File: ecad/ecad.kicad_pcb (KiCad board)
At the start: 4 copper layers, 87 x 83 mm, 82 parts, among them J1 JTAG, J2 USB_C, SW1 Cherry MX, SW10 RotaryEncoder_Switch, SW11 RotaryEncoder_Switch, SW12 Cherry MX, SW13 Cherry MX, SW14 Cherry MX, SW15 RESET, SW2 Cherry MX, SW3 Cherry MX, SW4 Cherry MX, SW5 Cherry MX, SW6 Cherry MX, SW7 Cherry MX, SW8 Cherry MX, SW9 Cherry MX, U1 AP2112K-3.3, U2 RP2040, U4 SN74LV1T34DBV, U5 W25Q128JVP, Y1 12MHz

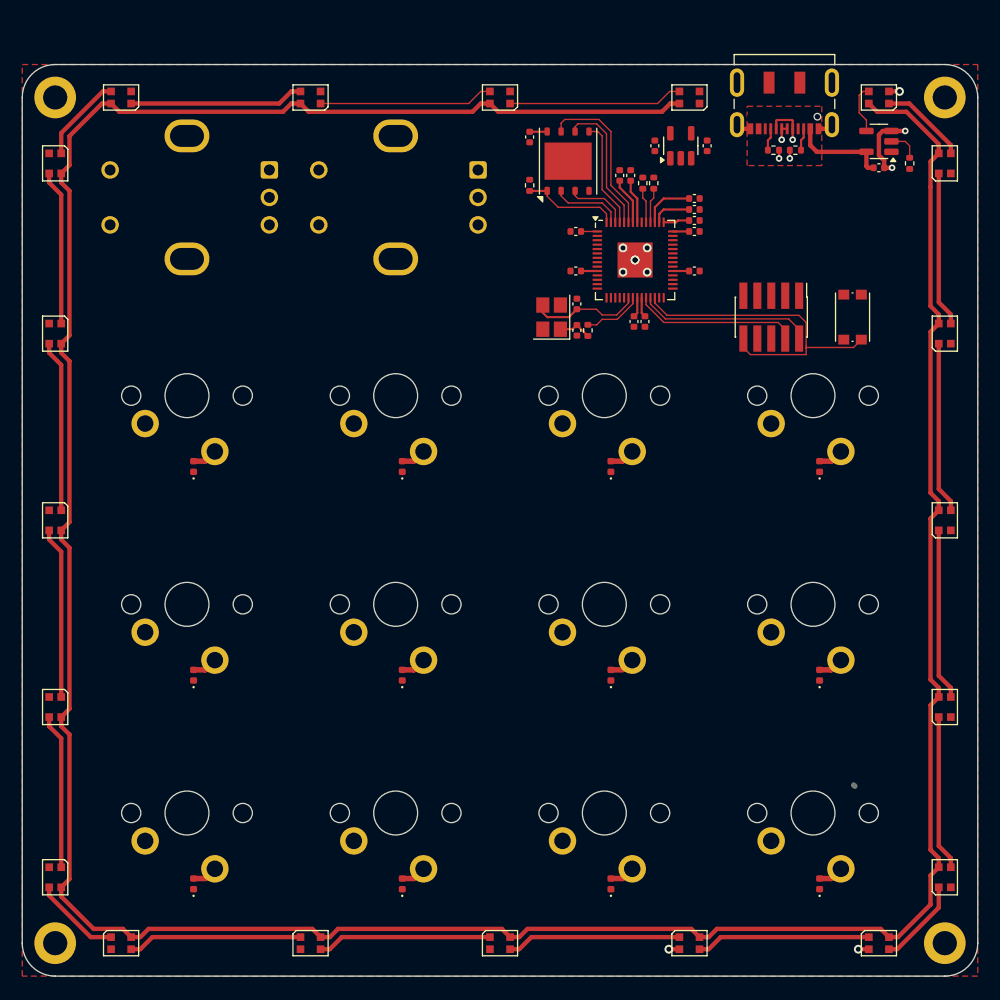
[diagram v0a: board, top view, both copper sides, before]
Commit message: feat(ecad): change pcb size to have constant margin
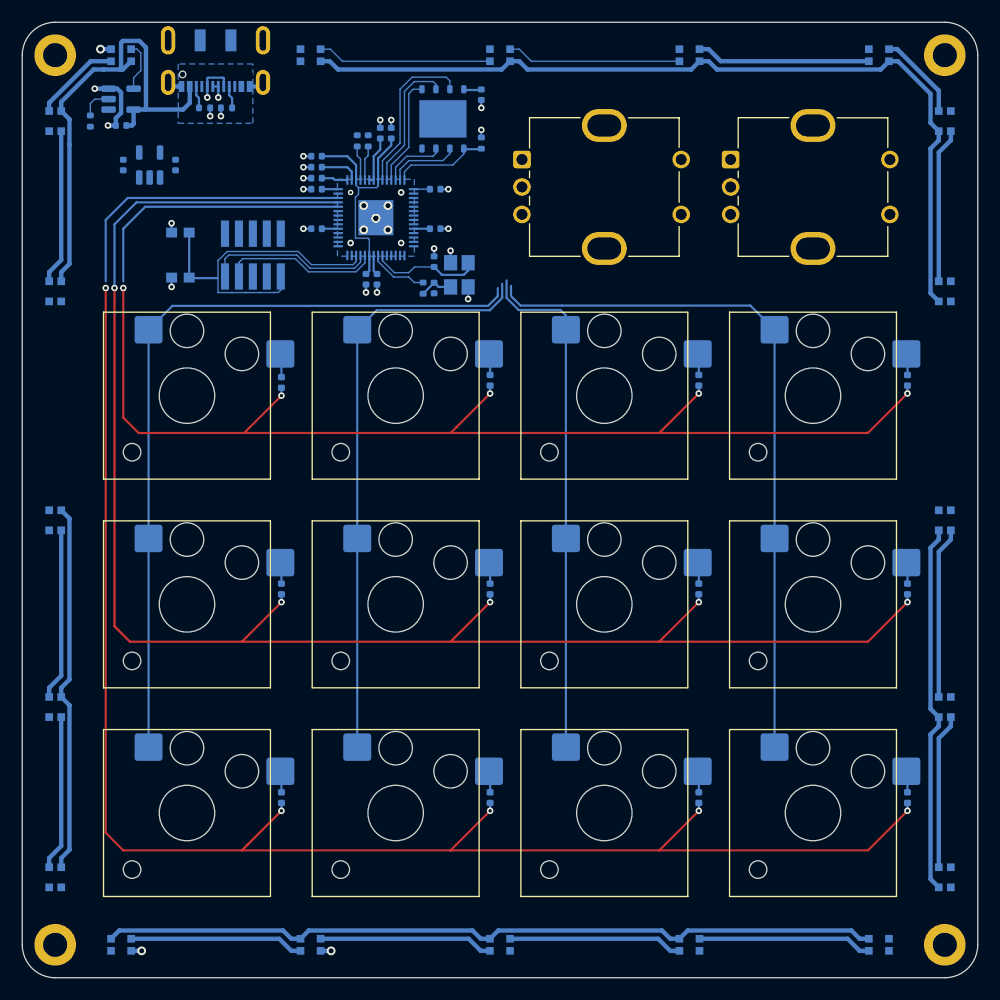
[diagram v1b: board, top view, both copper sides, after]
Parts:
- C1, C10, C11, C12, C13, C14, C15, C16, C17, C18, C2, C3, C4, C5, C6, C7, C8, D1, D10, D11, D12, D13, D14, D15, D16, D17, D18, D19, D2, D20, D21, D22, D23, D24, D25, D26, D27, D28, D29, D3, D30, D31, D32, D4, D5, D6, D7, D8, D9, H1, H2, H3, H4, J1, J2, R1, R2, R3, R4, R5, R6, R7, SW15, U1, U2, U4, U5, Y1: moved to B.Cu
- SW1, SW12, SW13, SW14, SW2, SW3, SW4, SW5, SW6, SW7, SW8, SW9: footprint PCM_Switch_Keyboard_Cherry_MX:SW_Cherry_MX_PCB_1.00u -> PCM_Switch_Keyboard_Hotswap_Kailh:SW_Hotswap_Kailh_Choc_V2; moved to F.Cu
- SW10, SW11: moved to F.Cu
- moved D15 81.1 mm to (147.0, 81.2)
- moved D19 81.1 mm to (147.0, 96.7)
- moved D25 81.1 mm to (66.0, 96.7)
- moved D29 81.1 mm to (66.0, 81.2)
- moved H1 81.1 mm to (147.0, 75.2), turned to 180 degrees
- moved H2 81.1 mm to (66.0, 75.2), turned to 180 degrees
- moved H3 81.0 mm to (147.0, 156.2), turned to 180 degrees
- moved H4 81.0 mm to (66.0, 156.2), turned to 180 degrees
- moved D13 81.0 mm to (66.0, 150.0)
- moved D17 81.0 mm to (66.0, 134.5)
- moved D21 81.0 mm to (66.0, 117.5)
- moved D23 81.0 mm to (147.0, 117.5)
- moved D27 81.0 mm to (147.0, 134.5)
- moved D31 81.0 mm to (147.0, 150.0)
- moved R7 74.7 mm to (69.2, 81.2)
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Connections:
- U2 pad 39: unconnected-(U2-GPIO27_ADC1-Pad39) -> Net-(D11-K)
- U2 pad 7: Net-(D11-K) -> unconnected-(U2-GPIO5-Pad7)
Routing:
- net Net-(D11-K): track 0.00 -> 150.2 mm, vias 0 -> 5
- net Net-(D12-K): track 0.00 -> 142.9 mm, vias 0 -> 5
- net Net-(D1-K): track 0.00 -> 103.1 mm, vias 0 -> 5
- net Net-(U2-GPIO3): track 0.15 -> 71.8 mm
- net Net-(U2-GPIO0): track 0.00 -> 64.2 mm
- net Net-(U2-GPIO2): track 0.00 -> 53.7 mm
- net Net-(U2-GPIO1): track 0.00 -> 47.0 mm
- net +5V: track 303.9 -> 261.9 mm
- net unconnected-(U2-GPIO28_ADC2-Pad40): track 0.00 -> 27.6 mm
- net unconnected-(U2-GPIO26_ADC0-Pad38): track 0.00 -> 25.2 mm
- net Net-(D21-DIN): track 15.6 -> 0.00 mm
- net Net-(D19-DIN): track 15.6 -> 0.00 mm
- net GND: track 13.6 -> 26.9 mm, vias 13 -> 30
- net +1V1: track 10.9 -> 21.6 mm
- net Net-(D13-DOUT): track 7.95 -> 0.00 mm
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- added copper zone on B.Cu, net +3.3V
- added copper zone on B.Cu, net +5V
- removed copper zone on F.Cu, net +5V
- removed copper zone on F.Cu, net GND
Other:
- board size 87 x 83 mm -> 87 x 87 mm

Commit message: fix(ecad): change pcb format
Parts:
- added D33: D_Small, Diode_SMD:D_0402_1005Metric, F.Cu at (253.5, 91.5)
- added D34: D_Small, Diode_SMD:D_0402_1005Metric, F.Cu at (253.5, 93.5)
- added D35: D_Small, Diode_SMD:D_0402_1005Metric, F.Cu at (253.5, 95.4)
- added D36: D_Small, Diode_SMD:D_0402_1005Metric, F.Cu at (253.5, 97.4)
- added H5: MountingHole, MountingHole:MountingHole_2.2mm_M2_DIN965_Pad, F.Cu at (151.7, 107.8)
- added H6: MountingHole, MountingHole:MountingHole_2.2mm_M2_DIN965_Pad, F.Cu at (173.4, 107.8)
- added H7: MountingHole, MountingHole:MountingHole_2.2mm_M2_DIN965_Pad, F.Cu at (173.4, 153.3)
- added H8: MountingHole, MountingHole:MountingHole_2.2mm_M2_DIN965_Pad, F.Cu at (151.7, 153.4)
- added SW16: Kailh choc v2, PCM_Switch_Keyboard_Hotswap_Kailh:SW_Hotswap_Kailh_Choc_V2, F.Cu at (78.2, 87.4)
- added SW17: Kailh choc v2, PCM_Switch_Keyboard_Hotswap_Kailh:SW_Hotswap_Kailh_Choc_V2, F.Cu at (135.2, 87.4)
- added SW18: Kailh choc v2, PCM_Switch_Keyboard_Hotswap_Kailh:SW_Hotswap_Kailh_Choc_V2, F.Cu at (116.2, 87.4)
- added SW19: Kailh choc v2, PCM_Switch_Keyboard_Hotswap_Kailh:SW_Hotswap_Kailh_Choc_V2, F.Cu at (97.2, 87.4)
- H1, H2, H3, H4: footprint MountingHole:MountingHole_2.2mm_M2_DIN965_Pad -> MountingHole:MountingHole_2.2mm_M2_DIN965
- SW1, SW12, SW13, SW14, SW2, SW3, SW4, SW5, SW6, SW7, SW8, SW9: value Cherry MX -> Kailh choc v2
- moved C18 229.6 mm to (301.2, 69.5)
- moved D13 229.6 mm to (295.2, 138.0)
- moved D14 229.6 mm to (301.2, 144.1)
- moved D15 229.6 mm to (376.2, 69.1)
- moved D16 229.6 mm to (370.2, 63.1)
- moved D17 229.6 mm to (295.2, 122.5)
- moved D18 229.6 mm to (318.5, 144.1)
- moved D19 229.6 mm to (376.2, 84.6)
- moved D20 229.6 mm to (353.0, 63.1)
- moved D21 229.6 mm to (295.2, 105.5)
- moved D22 229.6 mm to (335.8, 144.1)
- moved D23 229.6 mm to (376.2, 105.5)
- moved D24 229.6 mm to (335.8, 63.1)
- moved D25 229.6 mm to (295.2, 84.6)
- moved D26 229.6 mm to (353.0, 144.1)
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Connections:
- SW1 pad 1: Net-(U2-GPIO0) -> Net-(U2-GPIO8)
- SW10 pad A: Net-(U2-GPIO20) -> unconnected-(SW10-PadA)
- SW10 pad B: Net-(U2-GPIO21) -> unconnected-(SW10-PadB)
- SW10 pad S1: Net-(U2-GPIO19) -> unconnected-(SW10-PadS1)
- SW11 pad A: Net-(U2-GPIO23) -> unconnected-(SW11-PadA)
- SW11 pad B: Net-(U2-GPIO24) -> unconnected-(SW11-PadB)
- SW11 pad S1: Net-(U2-GPIO22) -> unconnected-(SW11-PadS1)
- SW12 pad 1: Net-(U2-GPIO3) -> Net-(U2-GPIO11)
- SW13 pad 1: Net-(U2-GPIO3) -> Net-(U2-GPIO11)
- SW14 pad 1: Net-(U2-GPIO3) -> Net-(U2-GPIO11)
- SW2 pad 1: Net-(U2-GPIO0) -> Net-(U2-GPIO8)
- SW3 pad 1: Net-(U2-GPIO0) -> Net-(U2-GPIO8)
- SW4 pad 1: Net-(U2-GPIO1) -> Net-(U2-GPIO9)
- SW5 pad 1: Net-(U2-GPIO1) -> Net-(U2-GPIO9)
- SW6 pad 1: Net-(U2-GPIO1) -> Net-(U2-GPIO9)
- SW7 pad 1: Net-(U2-GPIO2) -> Net-(U2-GPIO10)
- SW8 pad 1: Net-(U2-GPIO2) -> Net-(U2-GPIO10)
- SW9 pad 1: Net-(U2-GPIO2) -> Net-(U2-GPIO10)
- U2 pad 11: unconnected-(U2-GPIO8-Pad11) -> Net-(U2-GPIO8)
- U2 pad 12: unconnected-(U2-GPIO9-Pad12) -> Net-(U2-GPIO9)
- U2 pad 13: unconnected-(U2-GPIO10-Pad13) -> Net-(U2-GPIO10)
- U2 pad 14: unconnected-(U2-GPIO11-Pad14) -> Net-(U2-GPIO11)
- U2 pad 19: GND -> unconnected-(U2-TESTEN-Pad19)
- U2 pad 2: Net-(U2-GPIO0) -> Net-(D33-K)
- U2 pad 29: /led/DIN -> unconnected-(U2-GPIO18-Pad29)
- U2 pad 3: Net-(U2-GPIO1) -> unconnected-(U2-GPIO1-Pad3)
- U2 pad 30: Net-(U2-GPIO19) -> unconnected-(U2-GPIO19-Pad30)
- U2 pad 31: Net-(U2-GPIO20) -> unconnected-(U2-GPIO20-Pad31)
- U2 pad 32: Net-(U2-GPIO21) -> unconnected-(U2-GPIO21-Pad32)
- U2 pad 34: Net-(U2-GPIO22) -> unconnected-(U2-GPIO22-Pad34)
- U2 pad 35: Net-(U2-GPIO23) -> Net-(D1-K)
- U2 pad 36: Net-(U2-GPIO24) -> Net-(D11-K)
- U2 pad 37: unconnected-(U2-GPIO25-Pad37) -> Net-(D12-K)
- U2 pad 39: Net-(D11-K) -> unconnected-(U2-GPIO27_ADC1-Pad39)
- U2 pad 4: Net-(U2-GPIO2) -> unconnected-(U2-GPIO2-Pad4)
- U2 pad 5: Net-(U2-GPIO3) -> unconnected-(U2-GPIO3-Pad5)
- U2 pad 57: GND -> unconnected-(U2-GND-Pad57)
- U2 pad 6: Net-(D1-K) -> unconnected-(U2-GPIO4-Pad6)
- U2 pad 8: Net-(D12-K) -> unconnected-(U2-GPIO6-Pad8)
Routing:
- net +5V: track 261.9 -> 0.00 mm
- net Net-(D11-K): track 150.2 -> 0.00 mm, vias 5 -> 0
- net Net-(D12-K): track 142.9 -> 0.00 mm, vias 5 -> 0
- net Net-(D1-K): track 103.1 -> 0.00 mm, vias 5 -> 0
- net Net-(U2-GPIO3): track 71.8 -> 0.00 mm
- net Net-(U2-GPIO0): track 64.2 -> 0.00 mm
- net Net-(U2-GPIO2): track 53.7 -> 0.00 mm
- net Net-(U2-GPIO1): track 47.0 -> 0.00 mm
- net Net-(J2-D--PadA7): track 4.03 -> 46.5 mm, vias 1 -> 0
- net Net-(J2-D+-PadA6): track 1.50 -> 44.0 mm, vias 1 -> 0
- net unconnected-(U2-GPIO28_ADC2-Pad40): track 27.6 -> 0.00 mm
- net unconnected-(U2-GPIO26_ADC0-Pad38): track 25.2 -> 0.00 mm
- net RESET: track 30.8 -> 6.71 mm
- net Net-(D16-DOUT): track 15.9 -> 0.00 mm
- net Net-(D26-DOUT): track 15.9 -> 0.00 mm
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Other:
- board size 87 x 87 mm -> 116.2 x 87 mm

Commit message: fix(ecad): replace components to fit new format
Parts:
- removed H5, H6, H7, H8: MountingHole, MountingHole:MountingHole_2.2mm_M2_DIN965_Pad
- added D37: D_Small, Diode_SMD:D_0402_1005Metric, B.Cu at (102.3, 45.0)
- added D38: D_Small, Diode_SMD:D_0402_1005Metric, B.Cu at (100.3, 45.0)
- added D39: D_Small, Diode_SMD:D_0402_1005Metric, B.Cu at (98.4, 45.0)
- added D40: D_Small, Diode_SMD:D_0402_1005Metric, B.Cu at (96.4, 45.0)
- added REF**: TE_1-84952-2_1x12-1MP_P1.0mm_Horizontal, Connector_FFC-FPC:TE_1-84952-2_1x12-1MP_P1.0mm_Horizontal, B.Cu at (170.5, 137.6)
- added SW20: Kailh choc v2, PCM_Switch_Keyboard_Hotswap_Kailh:SW_Hotswap_Kailh_Choc_V2, F.Cu at (135.0, 86.9)
- added SW21: Kailh choc v2, PCM_Switch_Keyboard_Hotswap_Kailh:SW_Hotswap_Kailh_Choc_V2, F.Cu at (116.2, 86.9)
- added SW22: Kailh choc v2, PCM_Switch_Keyboard_Hotswap_Kailh:SW_Hotswap_Kailh_Choc_V2, F.Cu at (97.2, 86.9)
- added SW23: Kailh choc v2, PCM_Switch_Keyboard_Hotswap_Kailh:SW_Hotswap_Kailh_Choc_V2, F.Cu at (78.2, 86.9)
- D33, D34, D35, D36: moved to B.Cu
- moved SW15 242.7 mm to (204.1, 56.3), turned to 180 degrees
- moved J1 236.4 mm to (205.3, 65.9), turned to 180 degrees
- moved R2 89.7 mm to (214.2, 49.3)
- moved R3 89.7 mm to (215.2, 49.3)
- moved C11 89.7 mm to (210.7, 52.9)
- moved C12 89.7 mm to (210.7, 50.9)
- moved C3 89.7 mm to (210.7, 51.9)
- moved C6 89.7 mm to (210.7, 53.9)
- moved C13 89.7 mm to (217.3, 48.7)
- moved C8 89.7 mm to (216.3, 48.7)
- moved C17 89.6 mm to (225.5, 45.3)
- moved C5 89.6 mm to (210.5, 57.5)
- moved C7 89.6 mm to (221.3, 57.1)
- moved U2 89.6 mm to (215.9, 56.5)
- moved U5 89.6 mm to (222.0, 47.5)
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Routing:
- net Net-(U2-GPIO11): track 0.00 -> 123.5 mm
- net Net-(U2-GPIO10): track 0.00 -> 104.1 mm
- net Net-(U2-GPIO9): track 0.00 -> 84.8 mm
- net Net-(U2-GPIO8): track 0.00 -> 65.4 mm
- net Net-(J2-D--PadA7): track 46.5 -> 3.34 mm
- net Net-(J2-D+-PadA6): track 44.0 -> 3.34 mm
- net Net-(J1-SWCLK/TCK): track 0.00 -> 14.9 mm
- net RESET: track 6.71 -> 20.7 mm
- net Net-(J1-SWDIO/TMS): track 0.00 -> 13.4 mm
- net GND: track 22.8 -> 19.7 mm, vias 19 -> 25
- net +3.3V: track 22.6 -> 23.2 mm, vias 5 -> 6
- net unconnected-(U2-GND-Pad57): vias 6 -> 4
- removed copper zone on B.Cu, net +5V
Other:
- board size 116.2 x 87 mm -> 130.5 x 110 mm

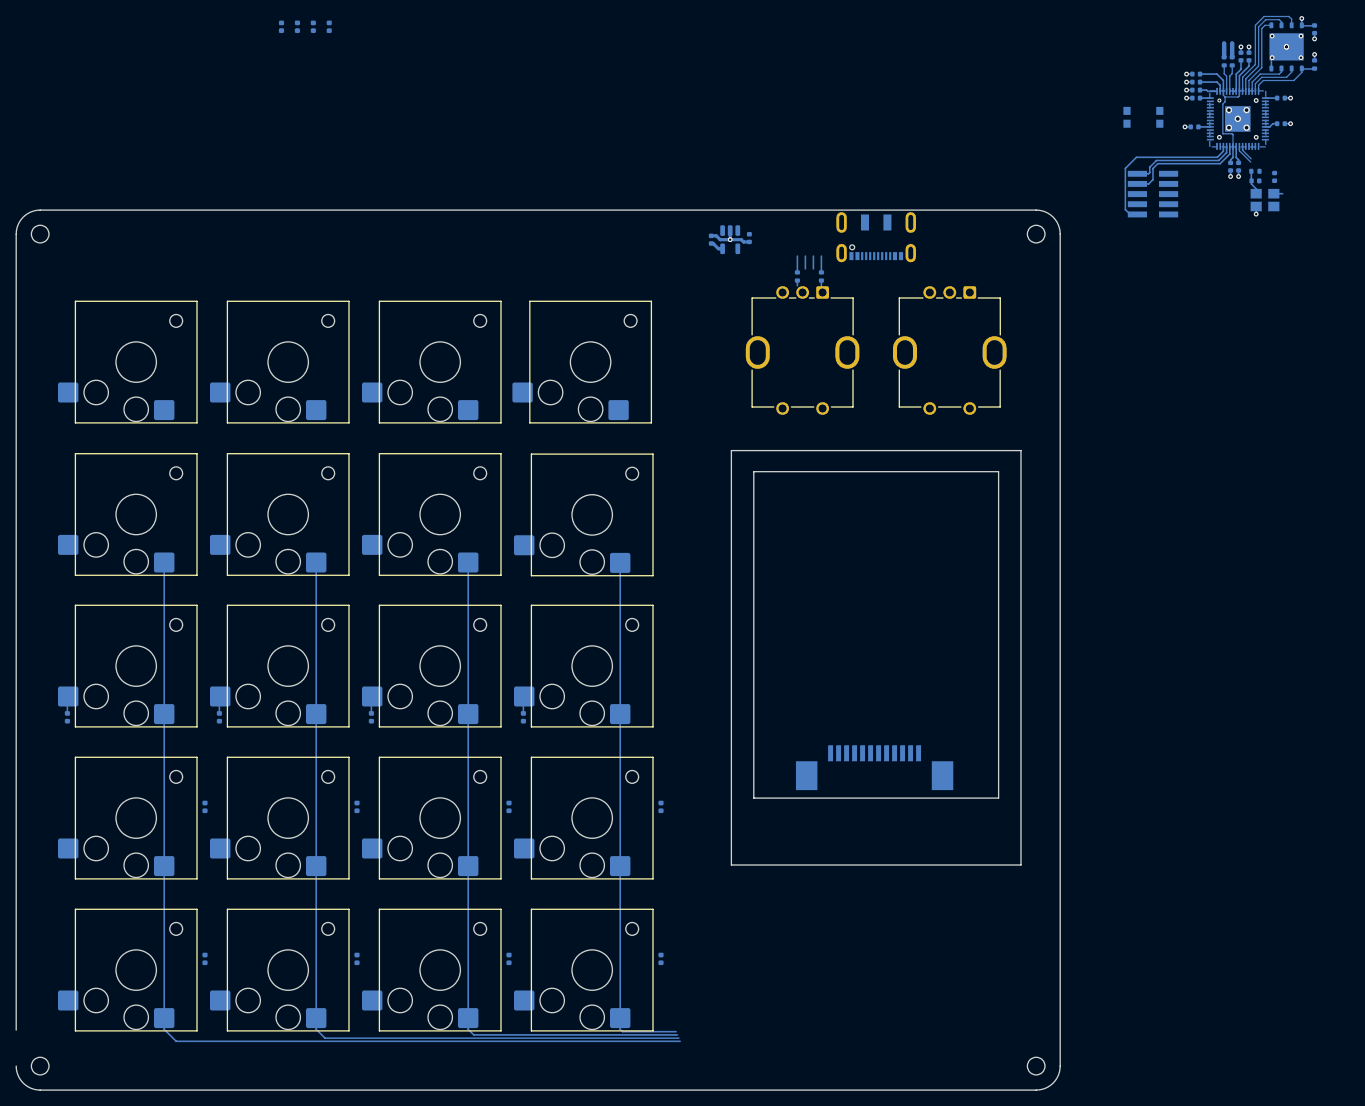
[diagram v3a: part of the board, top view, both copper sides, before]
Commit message: feat(ecad): add buttons, fpc connector, and holes to pass flexible pcb of display
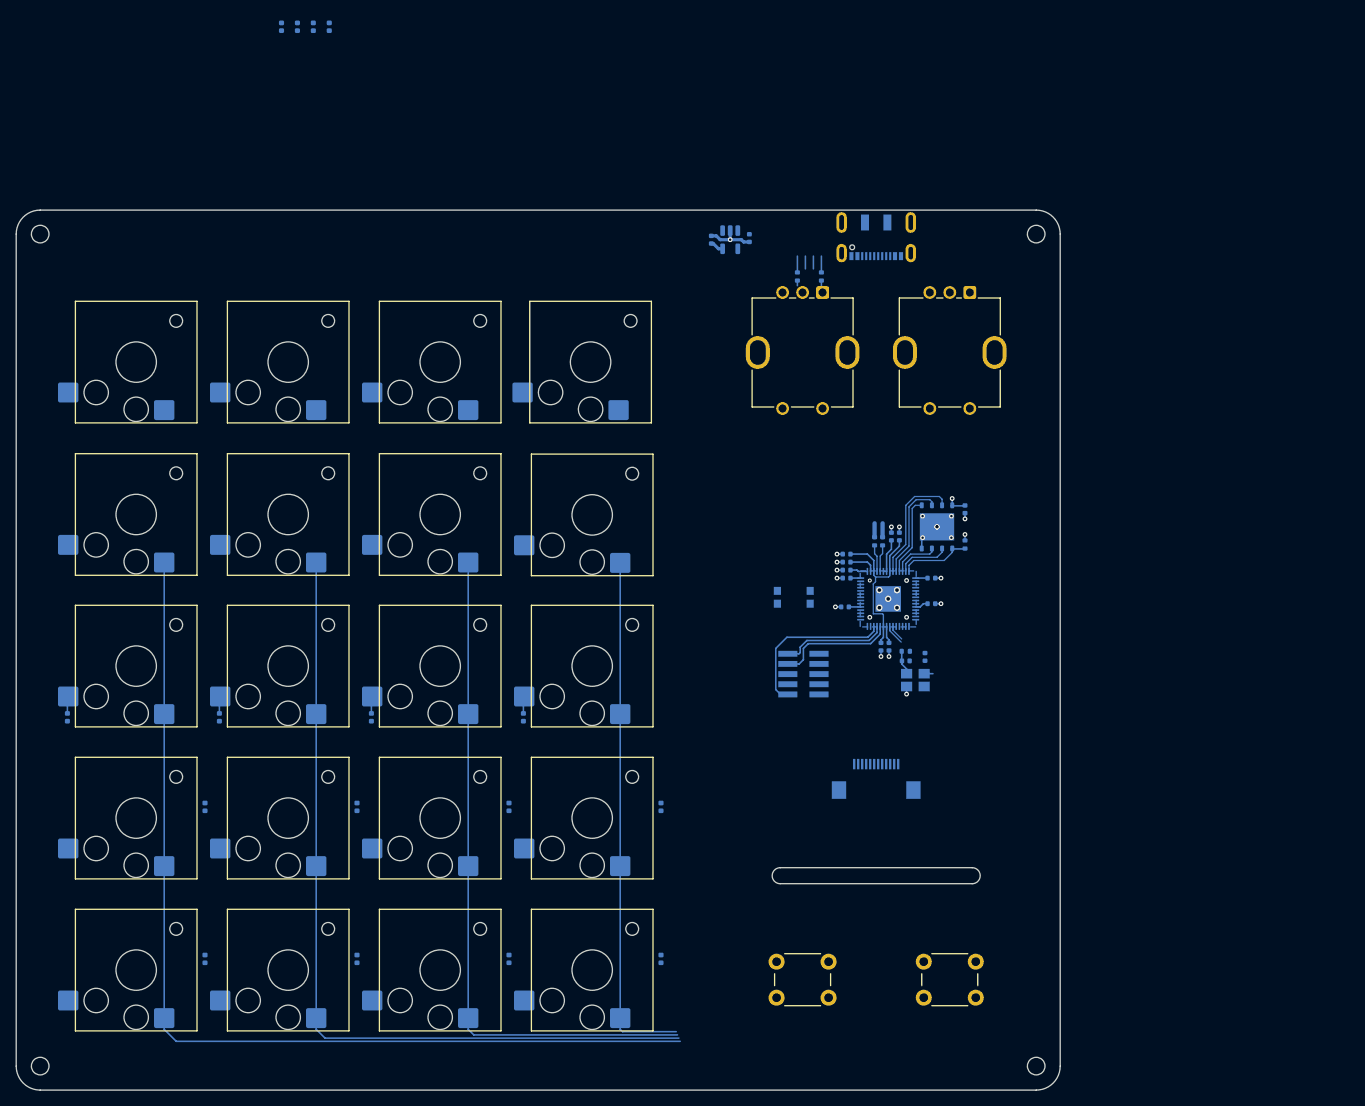
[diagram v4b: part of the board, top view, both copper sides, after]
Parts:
- removed REF**: TE_1-84952-2_1x12-1MP_P1.0mm_Horizontal, Connector_FFC-FPC:TE_1-84952-2_1x12-1MP_P1.0mm_Horizontal
- added J3: Display, Connector_FFC-FPC:Hirose_FH12-12S-0.5SH_1x12-1MP_P0.50mm_Horizontal, B.Cu at (170.7, 139.0)
- added SW24: Kailh choc v2, Button_Switch_THT:SW_PUSH_6mm, F.Cu at (176.7, 161.8)
- added SW25: Kailh choc v2, Button_Switch_THT:SW_PUSH_6mm, F.Cu at (158.2, 161.8)
- moved C10 74.2 mm to (177.6, 113.9)
- moved C11 74.2 mm to (167.0, 112.9)
- moved C12 74.2 mm to (167.0, 110.9)
- moved C13 74.2 mm to (173.6, 108.7)
- moved C14 74.2 mm to (171.3, 122.5)
- moved C3 74.2 mm to (167.0, 111.9)
- moved C4 74.2 mm to (172.3, 122.5)
- moved C6 74.2 mm to (167.0, 113.9)
- moved C7 74.2 mm to (177.6, 117.1)
- moved C8 74.2 mm to (172.6, 108.7)
- moved J1 74.2 mm to (161.6, 125.9)
- moved U2 74.2 mm to (172.2, 116.5)
- moved Y1 74.2 mm to (175.6, 126.7)
- moved C15 74.2 mm to (176.8, 123.8)
- moved C16 74.2 mm to (174.4, 124.2)
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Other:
- outline, holes or cut-outs redrawn
